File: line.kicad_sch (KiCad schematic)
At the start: 0 parts

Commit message: added more details to schematics
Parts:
- added D4, D5, D6, D7: LED, LED_SMD:LED_1210_3225Metric, symbol Device:LED
- added J10, J7, J8, J9: Screw_Terminal_01x03, symbol Connector:Screw_Terminal_01x03
- added R5, R6, R7, R8: 1k, Resistor_SMD:R_1210_3225Metric, symbol Device:R
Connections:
- new net: D5.2 (A), R6.1
- new net: D7.2 (A), R8.1
- new net: D6.2 (A), R7.1
- new net: D4.2 (A), R5.1
- new net +3.3V: J10.1 (Pin_1), J7.1 (Pin_1), J8.1 (Pin_1), J9.1 (Pin_1), R5.2, R6.2, R7.2, R8.2
- new net GND: J10.3 (Pin_3), J7.3 (Pin_3), J8.3 (Pin_3), J9.3 (Pin_3)
- new net LD_BACK_LEFT: D5.1 (K), J8.2 (Pin_2)
- new net LD_BACK_RIGHT: D7.1 (K), J10.2 (Pin_2)
- new net LD_FRONT_LEFT: D4.1 (K), J7.2 (Pin_2)
- new net LD_FRONT_RIGHT: D6.1 (K), J9.2 (Pin_2)
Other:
- note added: "Sensor Connection Reference"

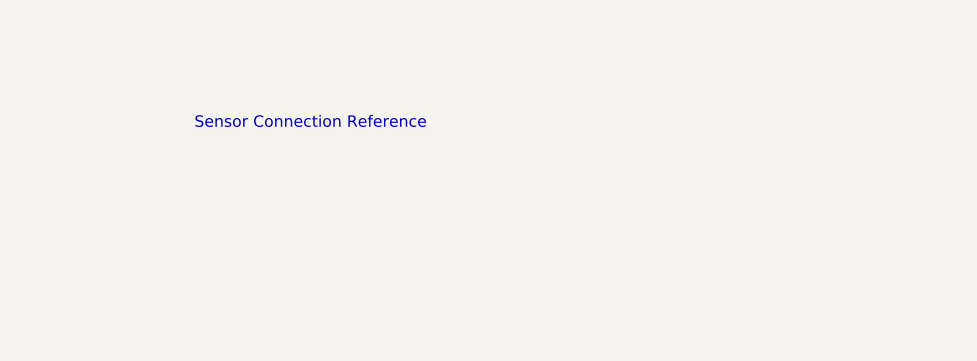
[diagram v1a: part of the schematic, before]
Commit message: started adding DC Motor controller logic
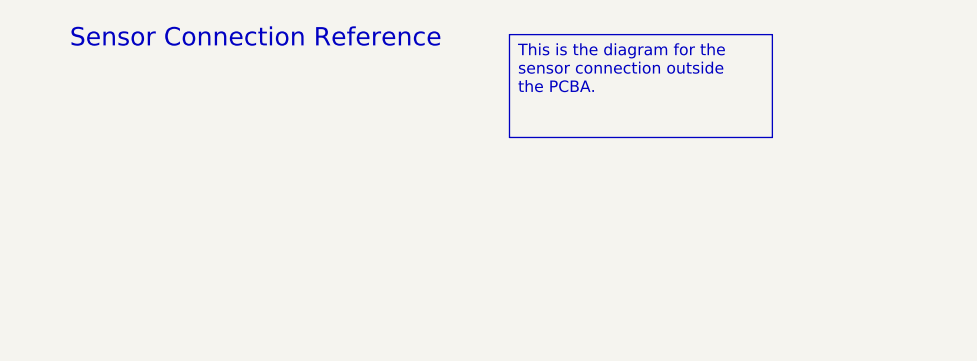
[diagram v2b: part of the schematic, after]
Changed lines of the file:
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@@
 	(text "Sensor Connection Reference "
 		(exclude_from_sim no)
-		(at 54.102 27.686 0)
+		(at 48.006 18.288 0)
+		(effects
+			(font
+				(size 2.032 2.032)
+			)
+		)
+	)
+	(text_box "This is the diagram for the sensor connection outside the PCBA. "
+		(exclude_from_sim no)
+		(at 76.2 17.78 0)
+		(size 29.21 11.43)
+		(margins 0.9525 0.9525 0.9525 0.9525)
+		(stroke
+			(width 0)
+			(type solid)
+		)
+		(fill
+			(type color)
+			(color 181 255 245 1)
+		)
 		(effects
 			(font
 				(size 1.27 1.27)
 			)
+			(justify left top)
 		)
 	)
@@
 	)
 	(image
-		(at 53.34 44.45)
-		(scale 0.276179)
+		(at 48.26 49.53)
+		(scale 0.526385)
 		(data "iVBORw0KGgoAAAANSUhEUgAAAWwAAAGFCAIAAABWtl6kAAAAA3NCSVQICAjb4U/gAAAACXBIWXMA"
 			"AA50AAAOdAFrJLPWAAAgAElEQVR4nO3df3gTZYIH8LcllFDbEmuBoWVrF6tMfVgvB1qiIhSM2vPu"

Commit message: added all footprints and step files to components
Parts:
- J10, J7, J8, J9: footprint (none) -> TerminalBlock_Phoenix:TerminalBlock_Phoenix_MKDS-1,5-3_1x03_P5.00mm_Horizontal
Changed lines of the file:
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@@
 			)
 		)
-		(property "Footprint" ""
+		(property "Footprint" "TerminalBlock_Phoenix:TerminalBlock_Phoenix_MKDS-1,5-3_1x03_P5.00mm_Horizontal"
 			(at 71.12 111.76 0)
 			(effects
@@
 			)
 		)
-		(property "Footprint" ""
+		(property "Footprint" "TerminalBlock_Phoenix:TerminalBlock_Phoenix_MKDS-1,5-3_1x03_P5.00mm_Horizontal"
 			(at 146.05 113.03 0)
 			(effects
@@
 			)
 		)
-		(property "Footprint" ""
+		(property "Footprint" "TerminalBlock_Phoenix:TerminalBlock_Phoenix_MKDS-1,5-3_1x03_P5.00mm_Horizontal"
 			(at 214.63 114.3 0)
 			(effects
@@
 			)
 		)
-		(property "Footprint" ""
+		(property "Footprint" "TerminalBlock_Phoenix:TerminalBlock_Phoenix_MKDS-1,5-3_1x03_P5.00mm_Horizontal"
 			(at 275.59 115.57 0)
 			(effects

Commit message: updated infomration on schematic; started working on layout
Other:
- company: (none) -> Erick Zamora 
- title: (none) -> Miniature Sumo Robot 
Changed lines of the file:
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@@
 	(generator_version "9.0")
 	(paper "A4")
+	(title_block
+		(title "Miniature Sumo Robot ")
+		(date "2025-09-26")
+		(rev "A")
+		(company "Erick Zamora ")
+	)
 	(text "Sensor Connection Reference "
 		(exclude_from_sim no)
